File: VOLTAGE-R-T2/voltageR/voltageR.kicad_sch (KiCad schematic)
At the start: 19 parts, among them U1 TPS56637RPAR, U2 TPS54202DDCR

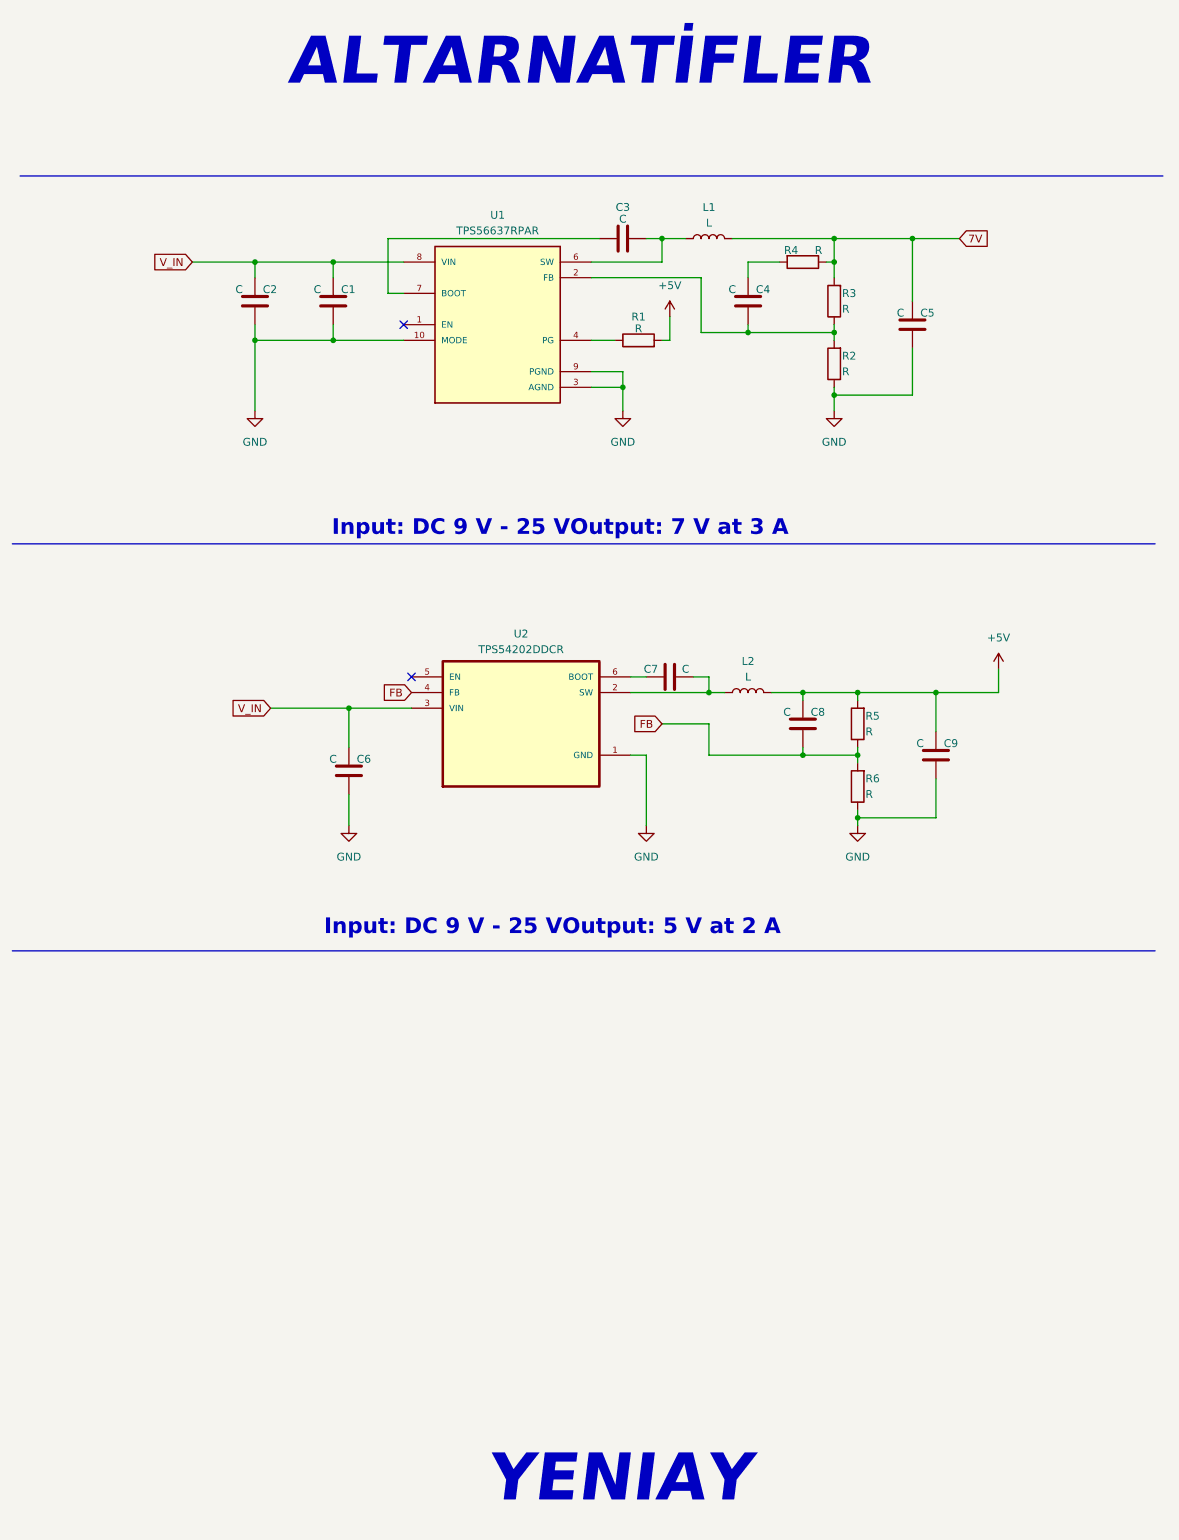
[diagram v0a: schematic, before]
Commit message: Voltage Regulator warnings are resolved
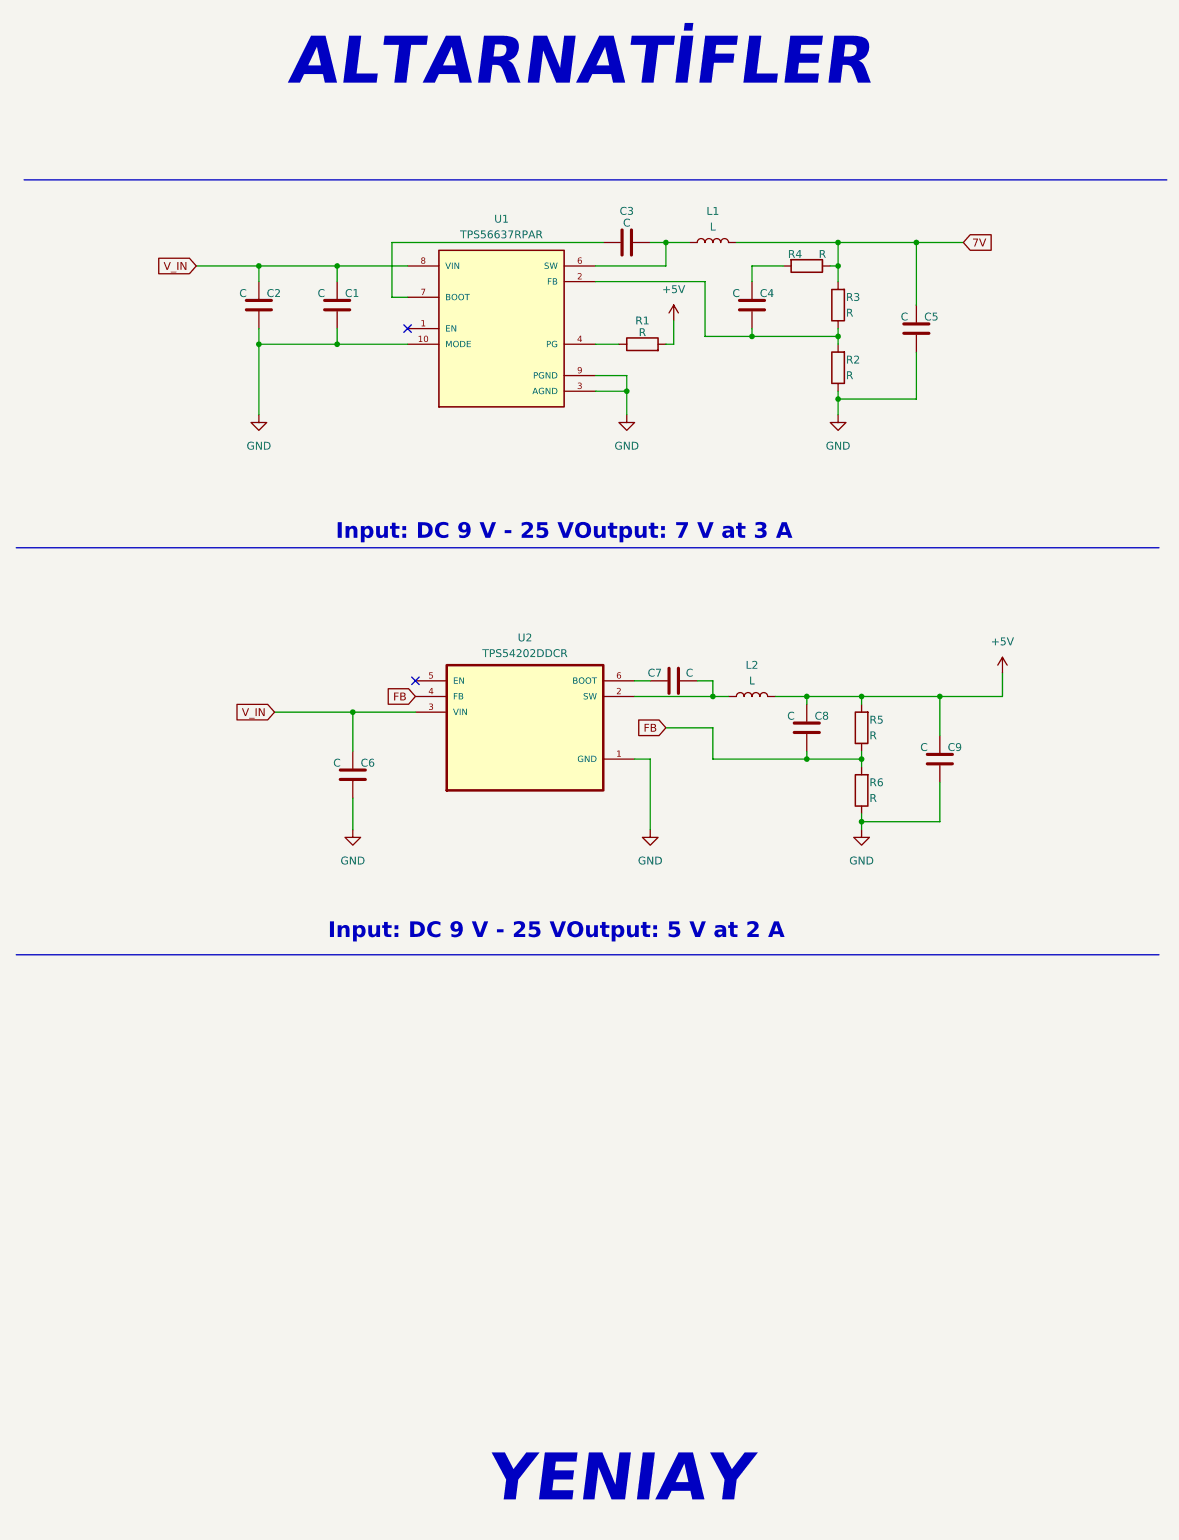
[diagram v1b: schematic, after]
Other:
- moved on the sheet: C1, C2, C3, C4, C5, C6, C7, C8, C9, L1, L2, R1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
